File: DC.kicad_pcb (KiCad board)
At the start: 2 copper layers, 3.5 x 26.1 mm, 24 parts, among them U6 MCP2551-I-P, U7 NUCLEO-F302R8

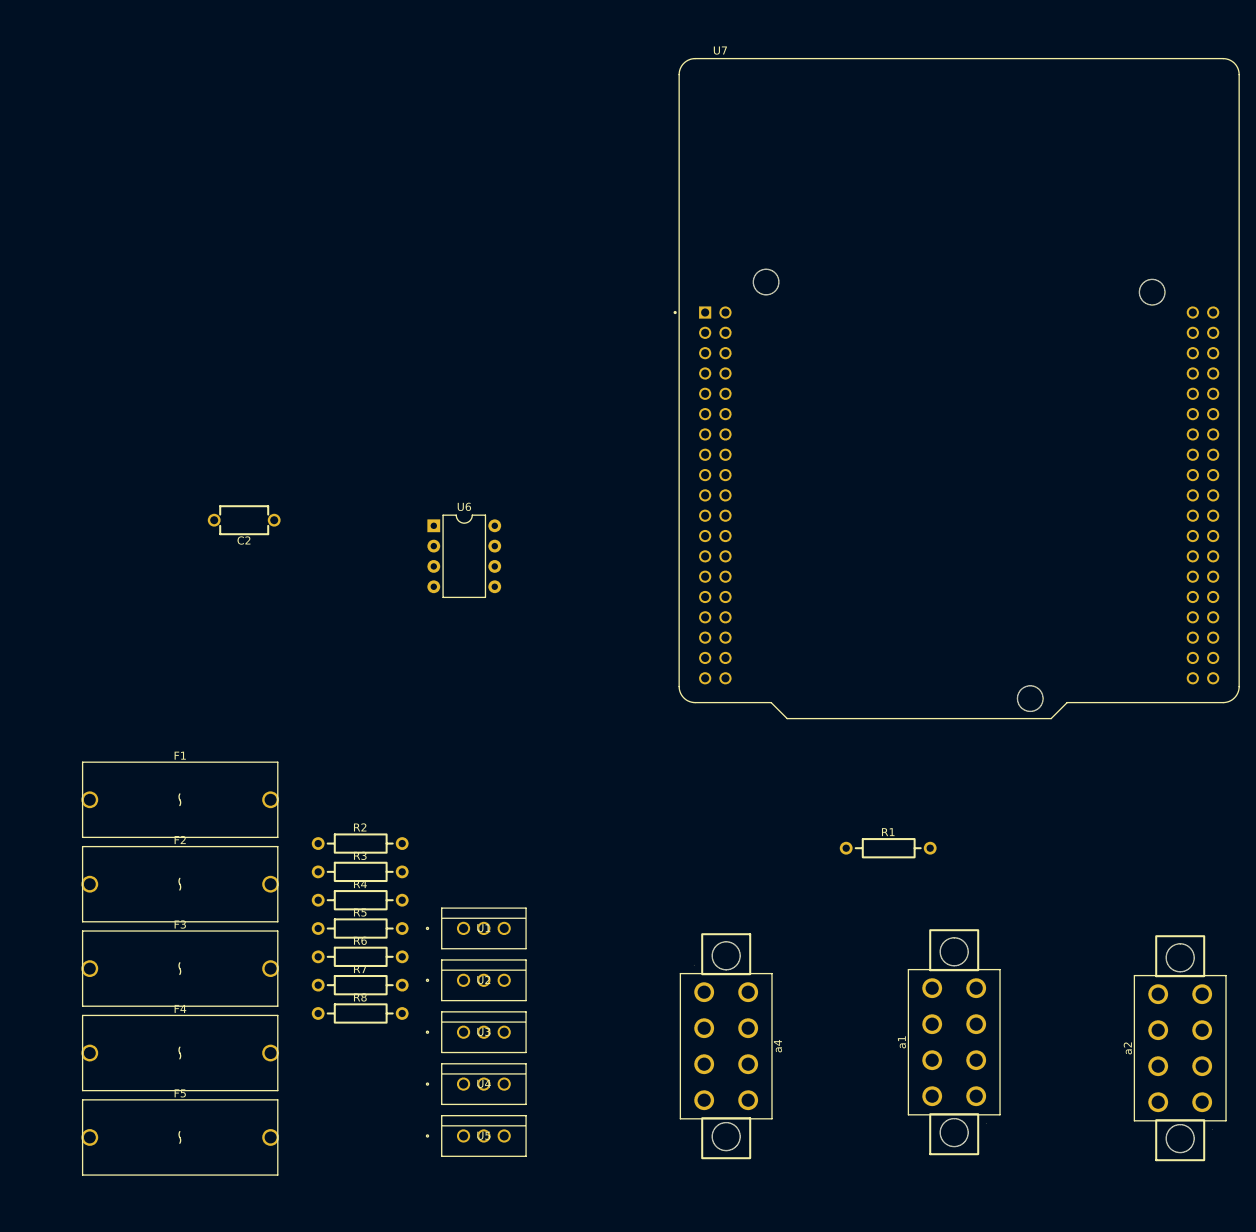
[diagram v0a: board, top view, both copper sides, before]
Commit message: pcb tolerances setup, component arrangement
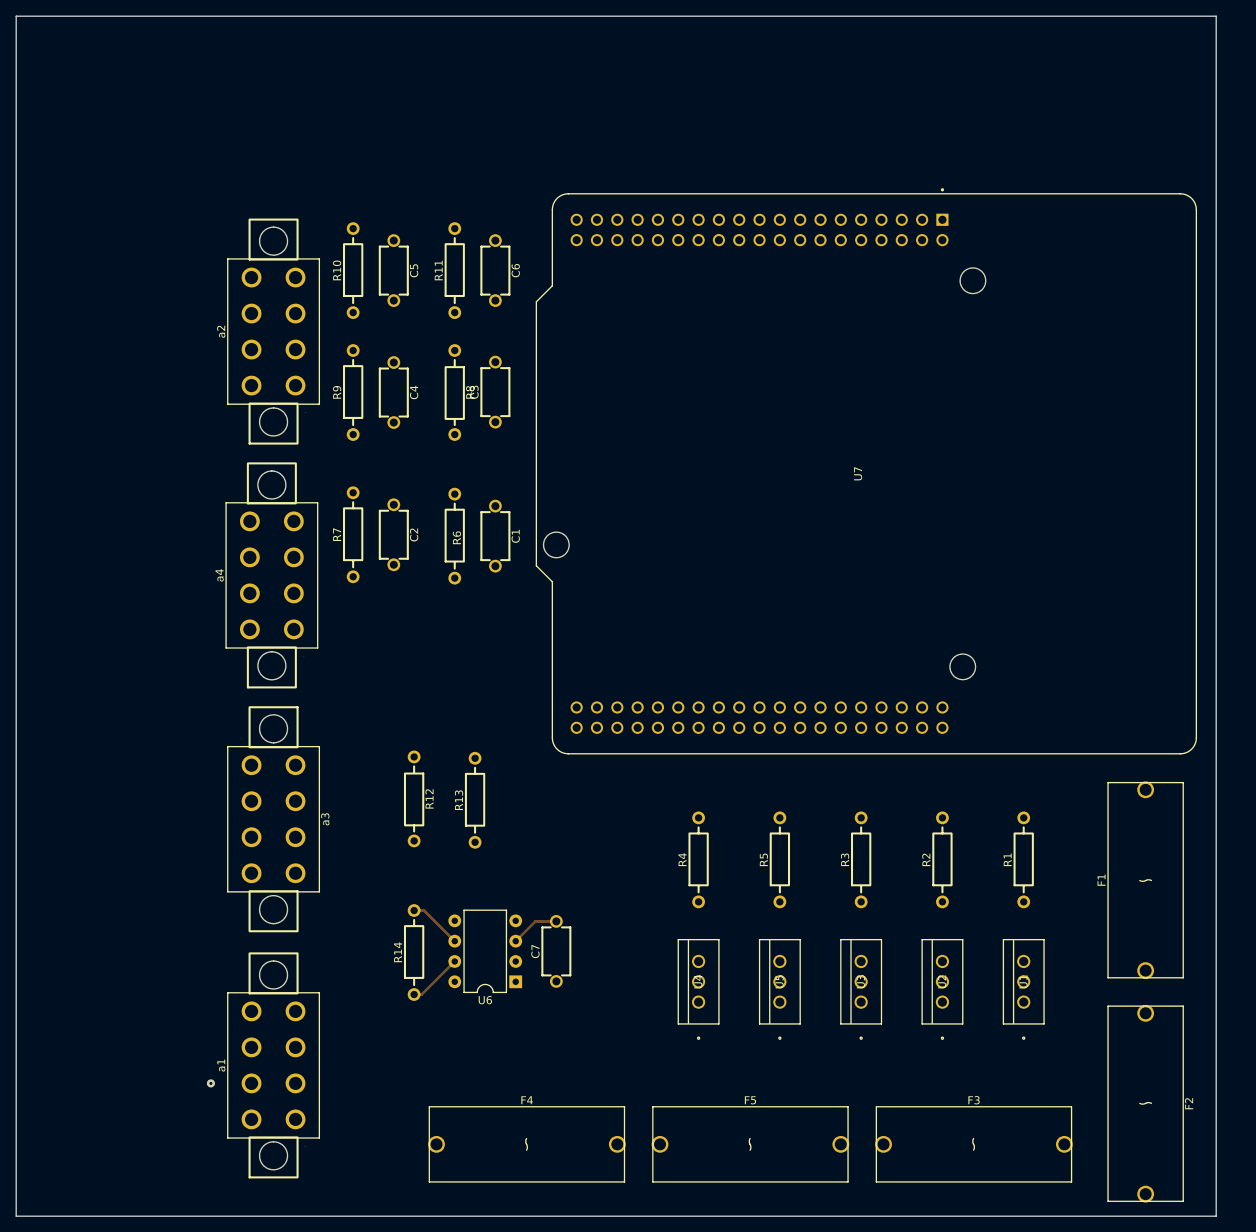
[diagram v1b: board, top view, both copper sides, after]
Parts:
- added C1: C, DriverControlsLib:CAP-TH_L6.0-W3.5-P7.50-D1.0, F.Cu at (88.9, 84.0)
- added C3: C, DriverControlsLib:CAP-TH_L6.0-W3.5-P7.50-D1.0, F.Cu at (88.9, 66.0)
- added C4: C, DriverControlsLib:CAP-TH_L6.0-W3.5-P7.50-D1.0, F.Cu at (76.2, 66.0)
- added C5: C, DriverControlsLib:CAP-TH_L6.0-W3.5-P7.50-D1.0, F.Cu at (76.2, 50.8)
- added C6: C, DriverControlsLib:CAP-TH_L6.0-W3.5-P7.50-D1.0, F.Cu at (88.9, 50.8)
- added C7: C, DriverControlsLib:CAP-TH_L6.0-W3.5-P7.50-D1.0, F.Cu at (96.5, 135.9)
- added R10: 10kΩ, DriverControlsLib:RES-TH_BD2.2-L6.5-P10.50-D0.6, F.Cu at (71.1, 50.8)
- added R11: 10kΩ, DriverControlsLib:RES-TH_BD2.2-L6.5-P10.50-D0.6, F.Cu at (83.8, 50.8)
- added R12: 12kΩ, DriverControlsLib:RES-TH_BD2.2-L6.5-P10.50-D0.6, F.Cu at (78.7, 116.8)
- added R13: 3.3kΩ, DriverControlsLib:RES-TH_BD2.2-L6.5-P10.50-D0.6, F.Cu at (86.4, 117.0)
- added R14: 120Ω, DriverControlsLib:RES-TH_BD2.2-L6.5-P10.50-D0.6, F.Cu at (78.7, 136.0)
- added R9: 10kΩ, DriverControlsLib:RES-TH_BD2.2-L6.5-P10.50-D0.6, F.Cu at (71.1, 66.0)
- added a3: ~, DriverControlsLib:Molex 8 Pin Mini-fit TPA, F.Cu at (61.2, 119.4)
- R1: value 12kΩ -> 220Ω
- R2: value 3.3kΩ -> 220Ω
- R3, R4, R5: value 1kΩ -> 220Ω
- R6, R7: value 1kΩ -> 10kΩ
- R8: value 120Ω -> 10kΩ
- moved a2 144.5 mm to (61.2, 58.4)
- moved F2 123.8 mm to (170.2, 154.9), turned to -90 degrees
- moved F1 121.1 mm to (170.2, 127.0), turned to 90 degrees
- moved F3 101.6 mm to (148.7, 160.0)
- moved a1 85.1 mm to (61.2, 150.1)
- moved a4 81.8 mm to (61.0, 88.9), turned to 90 degrees
- moved R8 78.5 mm to (83.8, 66.0), turned to -90 degrees
- moved R2 72.8 mm to (144.8, 124.5), turned to 90 degrees
- moved F5 71.3 mm to (120.8, 160.0)
- moved U1 70.6 mm to (154.9, 142.2), turned to 90 degrees
- moved R3 62.6 mm to (134.6, 124.5), turned to 90 degrees
- moved U2 59.9 mm to (144.8, 142.2), turned to 90 degrees
- moved U6 57.9 mm to (91.4, 139.7), turned to 180 degrees
- moved R7 56.3 mm to (71.1, 83.8), turned to 90 degrees
- moved R6 53.9 mm to (83.8, 84.0), turned to 90 degrees
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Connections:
- C2 pad 2: /CAN_Transceiver_5V -> /LSignalLightButton
- F1 pad 1: VCC -> /BrakeLightNeg
- F2 pad 1: VCC -> /RSignalLightNeg
- F3 pad 1: VCC -> /LSignalLightNeg
- F4 pad 1: VCC -> /DRLRightNeg
- F5 pad 1: VCC -> /DRLLeftNeg
- R1 pad 1: /SupBattery -> Net-(U1-G)
- R1 pad 2: /SupBattMonitor -> /BrakeLightOut
- R2 pad 1: /SupBattMonitor -> Net-(U2-G)
- R2 pad 2: GND -> /RSignalLightOut
- R3 pad 1: /BrakeLight_Out -> Net-(U3-G)
- R3 pad 2: GND -> /LSignalLightOut
- R4 pad 1: /RightSignalLight_Out -> Net-(U4-G)
- R4 pad 2: GND -> /DRLRightOut
- R5 pad 1: /LeftSignalLight_Out -> Net-(U5-G)
- R5 pad 2: GND -> /DRLLeftOut
- R6 pad 1: /DRL_Right_Out -> /RSignalLightButton
- R6 pad 2: GND -> /+3V3
- R7 pad 1: /DRL_Left_Out -> /LSignalLightButton
- R7 pad 2: GND -> /+3V3
- R8 pad 1: /CAN_H -> /AccelIn
- R8 pad 2: /CAN_L -> /+3V3
- U1 pad 1: /BrakeLight_Out -> Net-(U1-G)
- U1 pad 3: /BrakeLight_PWR -> GND
- U2 pad 1: /RightSignalLight_Out -> Net-(U2-G)
- U2 pad 3: /RightSignalLight_PWR -> GND
- U3 pad 1: /LeftSignalLight_Out -> Net-(U3-G)
- U3 pad 3: /LeftSignalLight_PWR -> GND
- U4 pad 1: /DRL_Right_Out -> Net-(U4-G)
- U4 pad 3: /DRL_Right_PWR -> GND
- U5 pad 1: /DRL_Left_Out -> Net-(U5-G)
- U5 pad 3: /DRL_Left_PWR -> GND
- U6 pad 3: /CAN_Transceiver_5V -> /CANTransceiver5V
- U7 pad CN10_1: /RightSignalLight_In -> /RSignalLightButton
- U7 pad CN10_2: /LeftSignalLight_In -> /LSignalLightButton
- U7 pad CN10_21: /BrakePedal_In -> /BrakePedal
- U7 pad CN10_22: /DI_Extra2 -> /DIExtra2
- U7 pad CN10_23: /Hazards_In -> /HazardButton
- U7 pad CN10_25: /DI_Extra1 -> /DIExtra1
- U7 pad CN10_27: /DRL_Right_Out -> /DRLRightOut
- U7 pad CN10_29: /DO_Extra1 -> /DOExtra1
- U7 pad CN7_1: /LeftSignalLight_Out -> /LSignalLightOut
- U7 pad CN7_18: /CAN_Transceiver_+5V -> /CANTransceiver5V
- U7 pad CN7_2: /RightSignalLight_Out -> /RSignalLightOut
- U7 pad CN7_3: /BrakeLight_Out -> /BrakeLightOut
- U7 pad CN7_32: /Acceleration -> /AccelIn
- U7 pad CN7_4: /DRL_Left_Out -> /DRLLeftOut
- a1 pad 1: /RightSignalLight_In -> /BrakeLightNeg
- a1 pad 2: /LeftSignalLight_In -> /RSignalLightNeg
- a1 pad 3: /Acceleration -> /LSignalLightNeg
- a1 pad 4: /BrakePedal_In -> /DRLRightNeg
- a1 pad 5: /UART_TX -> /DRLLeftNeg
- a1 pad 6: /UART_RX -> GND
- a1 pad 7: /ThermalShutoff -> GND
- a1 pad 8: /DI_Extra1 -> GND
- a2 pad 1: /Hazards_In -> /RSignalLightButton
- a2 pad 2: /Neutral -> /LSignalLightButton
- a2 pad 3: /Drive -> AccelPedal
- a2 pad 4: /Reverse -> /BrakePedal
- a2 pad 5: /SupBattery -> /GearSelector
- a2 pad 6: /DI_Extra2 -> /HazardButton
- a2 pad 7: VCC -> unconnected-(a2-Pad7)
- a2 pad 8: GND -> unconnected-(a2-Pad8)
- a4 pad 1: /BrakeLight_PWR -> /DIExtra1
- a4 pad 2: /RightSignalLight_PWR -> /DIExtra2
- a4 pad 3: /LeftSignalLight_PWR -> /DOExtra1
- a4 pad 4: /DRL_Right_PWR -> /ThermalShutoff
- a4 pad 5: /DRL_Left_PWR -> /UART_TX
- a4 pad 6: /DO_Extra1 -> /UART_RX
- a4 pad 7: GND -> unconnected-(a4-Pad7)
- a4 pad 8: GND -> unconnected-(a4-Pad8)
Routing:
- net GND: track 0.00 -> 18.4 mm, vias 0 -> 1
- net /CAN_H: track 0.00 -> 6.79 mm
- net /CAN_L: track 0.00 -> 6.67 mm
- net /CANTransceiver5V: track 0.00 -> 6.10 mm
- added copper zone on In1.Cu, net /+3V3
- added copper zone on In2.Cu, net GND
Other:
- board size 3.5 x 26.1 mm -> 150 x 150 mm
- copper layers 2 -> 4

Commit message: pcb routing, reassignment of stm32 pins
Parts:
- added F6: ~, DriverControlsLib:FUSE-TH_BD5.4-W22.5-P27.5-D0.8, F.Cu at (176.5, 132.1)
- moved F3 55.0 mm to (94.0, 154.9)
- moved C1 40.5 mm to (88.9, 124.5), turned to 90 degrees
- moved R6 40.5 mm to (83.8, 124.5)
- moved F5 29.5 mm to (149.9, 154.9)
- moved F4 29.5 mm to (121.9, 154.9)
- moved C2 28.4 mm to (88.9, 109.2), turned to 90 degrees
- moved R7 28.4 mm to (83.8, 109.2)
- moved F2 28.2 mm to (153.7, 132.1), turned to 90 degrees
- moved C3 28.0 mm to (88.9, 94.0), turned to -90 degrees
- moved R8 28.0 mm to (83.8, 94.0), turned to 90 degrees
- moved U3 23.4 mm to (111.8, 137.2), turned to -90 degrees
- moved R3 22.9 mm to (111.8, 124.5)
- moved R12 19.3 mm to (96.5, 124.5)
- moved C4 18.0 mm to (88.9, 78.7)
- moved R9 18.0 mm to (83.8, 78.7)
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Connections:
- U7 pad CN10_15: /Neutral -> unconnected-(U7B-PB15-PadCN10_15)
- U7 pad CN10_16: unconnected-(U7B-PB12-PadCN10_16) -> /DRLRightOut
- U7 pad CN10_18: unconnected-(U7B-PB11-PadCN10_18) -> /LSignalLightOut
- U7 pad CN10_19: /Drive -> unconnected-(U7B-PC7-PadCN10_19)
- U7 pad CN10_2: /LSignalLightButton -> /BrakeLightOut
- U7 pad CN10_22: /DIExtra2 -> /SupBattMonitor
- U7 pad CN10_23: /HazardButton -> /AccelIn
- U7 pad CN10_24: unconnected-(U7B-PB1-PadCN10_24) -> /RSignalLightButton
- U7 pad CN10_25: /DIExtra1 -> /LSignalLightButton
- U7 pad CN10_26: unconnected-(U7B-PA7-PadCN10_26) -> /Drive
- U7 pad CN10_27: /DRLRightOut -> unconnected-(U7B-PB4-PadCN10_27)
- U7 pad CN10_28: unconnected-(U7B-PA6-PadCN10_28) -> /Neutral
- U7 pad CN10_30: unconnected-(U7B-PA5-PadCN10_30) -> /Reverse
- U7 pad CN10_33: unconnected-(U7B-PA10-PadCN10_33) -> /ThermalShutoff
- U7 pad CN10_4: /Reverse -> /RSignalLightOut
- U7 pad CN10_6: unconnected-(U7B-PC5-PadCN10_6) -> /DRLLeftOut
- U7 pad CN7_1: /LSignalLightOut -> unconnected-(U7A-PC10-PadCN7_1)
- U7 pad CN7_17: /ThermalShutoff -> unconnected-(U7A-PA15-PadCN7_17)
- U7 pad CN7_2: /RSignalLightOut -> unconnected-(U7A-PC11-PadCN7_2)
- U7 pad CN7_24: VCC -> Net-(U7A-VIN)
- U7 pad CN7_3: /BrakeLightOut -> unconnected-(U7A-PC12-PadCN7_3)
- U7 pad CN7_32: /AccelIn -> unconnected-(U7A-PA4-PadCN7_32)
- U7 pad CN7_38: /SupBattMonitor -> /HazardButton
- U7 pad CN7_4: /DRLLeftOut -> unconnected-(U7A-PD2-PadCN7_4)
- a2 pad 3: AccelPedal -> /AccelIn
- a2 pad 5: /GearSelector -> /HazardButton
- a2 pad 6: /HazardButton -> /GearSelector
- a3 pad 1: /Drive -> /SupBattery
- a3 pad 2: /Neutral -> /Drive
- a3 pad 3: /Reverse -> /Neutral
- a3 pad 4: /SupBattery -> /Reverse
- a3 pad 5: unconnected-(a3-Pad5) -> /CAN_L
- a3 pad 6: unconnected-(a3-Pad6) -> /CAN_H
- a4 pad 5: /UART_TX -> /UART_RX
- a4 pad 6: /UART_RX -> /UART_TX
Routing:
- net VCC: track 0.00 -> 176.4 mm
- net /CANTransceiver5V: track 6.10 -> 145.3 mm, vias 0 -> 2
- net /RSignalLightButton: track 0.00 -> 121.0 mm, vias 0 -> 1
- net /RSignalLightNeg: track 0.00 -> 120.5 mm
- net /BrakeLightNeg: track 0.00 -> 113.6 mm
- net /LSignalLightButton: track 0.00 -> 104.2 mm, vias 0 -> 1
- net Net-(U7A-VIN): track 0.00 -> 97.7 mm
- net /AccelIn: track 0.00 -> 92.7 mm, vias 0 -> 1
- net /BrakePedal: track 0.00 -> 91.6 mm, vias 0 -> 1
- net /DRLLeftNeg: track 0.00 -> 90.8 mm
- net /UART_TX: track 0.00 -> 86.0 mm, vias 0 -> 1
- net /UART_RX: track 0.00 -> 75.3 mm, vias 0 -> 1
- net /CAN_TX: track 0.00 -> 71.2 mm, vias 0 -> 2
- net /ThermalShutoff: track 0.00 -> 57.7 mm, vias 0 -> 1
- net /HazardButton: track 0.00 -> 54.5 mm
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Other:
- board size 150 x 150 mm -> 439.6 x 166.8 mm
- board text added: "1"
- board text added: "2"
- board text added: "3"
- board text added: "4"
- board text added: "5"
- board text added: "6"
- board text added: "7"
- board text added: "8"
- board text added: "CAN VCC Gear"
- board text added: "CANH"
- board text added: "CANL"
- board text added: "Extra Pins"
- board text added: "Lights"
- board text added: "VCC"
- board text added: "to Buttons"
- board text added: "~"

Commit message: finished first draft of routing
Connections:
- U7 pad CN10_29: /DOExtra1 -> unconnected-(U7B-PB5-PadCN10_29)
- U7 pad CN7_32: unconnected-(U7A-PA4-PadCN7_32) -> /DIExtra1
- U7 pad CN7_34: unconnected-(U7A-PB0-PadCN7_34) -> /DIExtra2
- U7 pad CN7_36: unconnected-(U7A-PC1-PadCN7_36) -> /DOExtra1
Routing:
- net /DIExtra1: track 0.00 -> 70.5 mm, vias 0 -> 1
- net /DIExtra2: track 0.00 -> 66.1 mm, vias 0 -> 1
- net /DOExtra1: track 0.00 -> 62.1 mm, vias 0 -> 1
- net /ThermalShutoff: track 57.7 -> 60.0 mm
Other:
- board size 439.6 x 166.8 mm -> 125 x 125 mm

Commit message: fixed labels
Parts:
- moved C1 1.27 mm to (90.2, 124.5)
- moved C2 1.27 mm to (90.2, 109.2)
- moved C3 1.27 mm to (90.2, 94.0)
- moved C4 1.27 mm to (90.2, 78.7)
- moved C5 1.27 mm to (90.2, 48.3)
- moved C6 1.27 mm to (90.2, 63.5)
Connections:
- U7 pad CN10_1: /RSignalLightButton -> unconnected-(U7B-PC9-PadCN10_1)
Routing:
- net /GearSelector: track 44.2 -> 45.5 mm
- net /LSignalLightButton: track 104.2 -> 103.1 mm
